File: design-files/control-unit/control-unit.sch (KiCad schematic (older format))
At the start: 88 parts, among them SW501 SW_Push, U501 74HCT04, U502 74HCT161, U503 AT28C64, U504 AT28C64, U505 74HCT273, U506 74HCT377, U507 4002, U508 74HCT32, U509 AT28C64, U510 74HCT08, U511 74HCT157, U512 AT28C64, U513 74HCT173, U514 74HCT173, U515 74HCT08

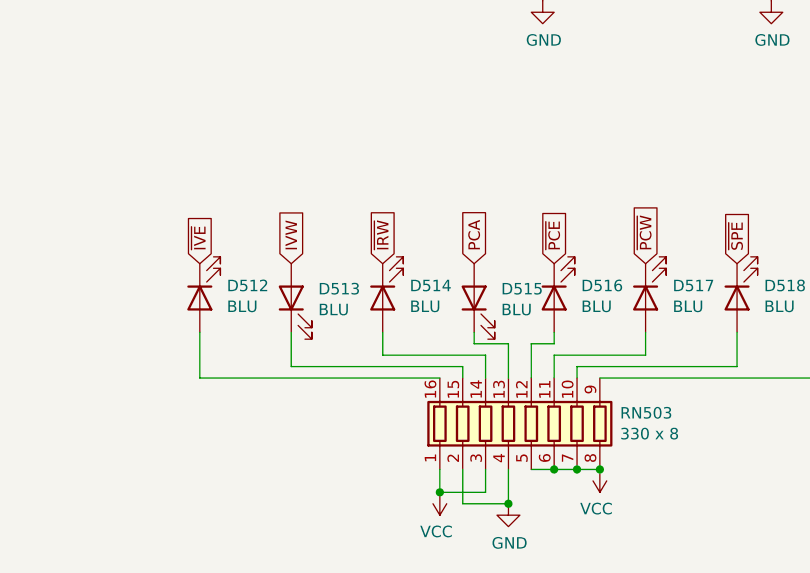
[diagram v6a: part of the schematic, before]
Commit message: Oops, fix the _IVW indicator LED; it's an active-low signal now.
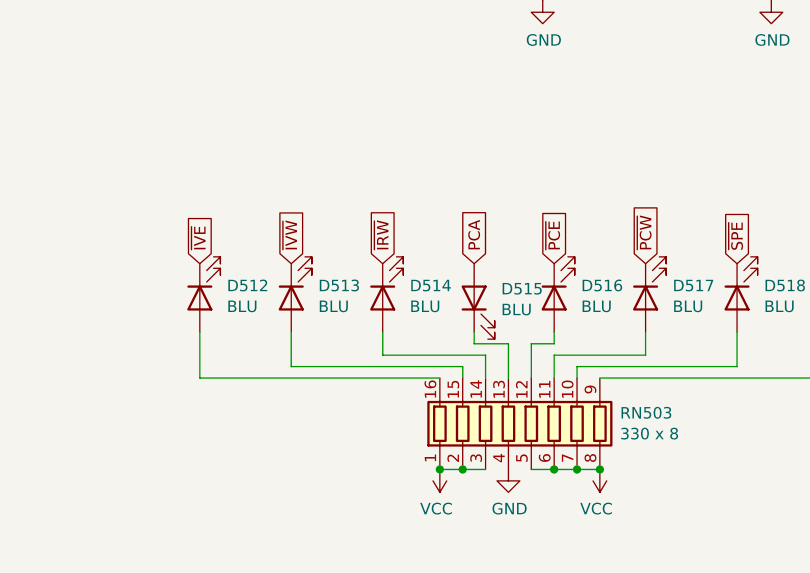
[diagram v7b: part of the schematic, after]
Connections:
- net IVW is gone; now on an unnamed net: D513.2 (A)
- net GND: no longer RN503.2 (R2.1)
- net VCC: now also RN503.2 (R2.1)
- net ~IVW: now also D513.1 (K)
- net at RN503.15 (R2.2): no longer D513.1 (K)
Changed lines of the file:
@@
-$EndComp
-$Comp
-L Device:LED D513
-U 1 1 6325CACA
-P 5450 7750
-F 0 "D513" V 5489 7632 50  0000 R CNN
-F 1 "BLU" V 5398 7632 50  0000 R CNN
-F 2 "LED_THT:LED_D5.0mm" H 5450 7750 50  0001 C CNN
-F 3 "~" H 5450 7750 50  0001 C CNN
-	1    5450 7750
-	0    -1   -1   0
 $EndComp
 $Comp
@@
 L power:GND #PWR0178
 U 1 1 6325CAF4
-P 6400 8650
-F 0 "#PWR0178" H 6400 8400 50  0001 C CNN
-F 1 "GND" H 6405 8477 50  0000 C CNN
-F 2 "" H 6400 8650 50  0001 C CNN
-F 3 "" H 6400 8650 50  0001 C CNN
-	1    6400 8650
+P 6400 8500
+F 0 "#PWR0178" H 6400 8250 50  0001 C CNN
+F 1 "GND" H 6405 8327 50  0000 C CNN
+F 2 "" H 6400 8500 50  0001 C CNN
+F 3 "" H 6400 8500 50  0001 C CNN
+	1    6400 8500
 	1    0    0    -1
 $EndComp
@@
 ~IVE
 Text GLabel 5450 7600 1    50   Input ~ 0
-IVW
+~IVW
 Text GLabel 5850 7600 1    50   Input ~ 0
 ~IRW
@@
 L power:VCC #PWR0198
 U 1 1 6399C3BB
-P 6100 8600
-F 0 "#PWR0198" H 6100 8450 50  0001 C CNN
-F 1 "VCC" H 6115 8773 50  0000 C CNN
-F 2 "" H 6100 8600 50  0001 C CNN
-F 3 "" H 6100 8600 50  0001 C CNN
-	1    6100 8600
+P 6100 8500
+F 0 "#PWR0198" H 6100 8350 50  0001 C CNN
+F 1 "VCC" H 6115 8673 50  0000 C CNN
+F 2 "" H 6100 8500 50  0001 C CNN
+F 3 "" H 6100 8500 50  0001 C CNN
+	1    6100 8500
 	-1   0    0    1
 $EndComp
@@
 Connection ~ 6800 8500
 Wire Wire Line
-	6300 8500 6300 8600
-Wire Wire Line
-	6300 8600 6100 8600
-Wire Wire Line
-	6100 8600 6100 8500
-Connection ~ 6100 8600
-Wire Wire Line
-	6200 8500 6200 8650
-Wire Wire Line
-	6200 8650 6400 8650
-Wire Wire Line
-	6400 8650 6400 8500
-Connection ~ 6400 8650
-Wire Wire Line
 	2650 8500 2550 8500
 Wire Wire Line
@@
 	12650 5300 13150 5300
 Connection ~ 13150 5300
+$Comp
+L Device:LED D513
+U 1 1 66E12AAA
+P 5450 7750
+F 0 "D513" V 5397 7632 50  0000 R CNN
+F 1 "BLU" V 5488 7632 50  0000 R CNN
+F 2 "LED_THT:LED_D5.0mm" H 5450 7750 50  0001 C CNN
+F 3 "~" H 5450 7750 50  0001 C CNN
+	1    5450 7750
+	0    -1   1    0
+$EndComp
+Wire Wire Line
+	6300 8500 6200 8500
+Wire Wire Line
+	6200 8500 6100 8500
+Connection ~ 6200 8500
+Connection ~ 6100 8500
 $EndSCHEMATC
